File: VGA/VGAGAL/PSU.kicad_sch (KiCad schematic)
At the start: 33 parts, among them U10 74LVC10, U11 74LVC11, U12 SN74LVC86, U16 74VLC1008, U17 74LVC139, U18 74LVC11, U19 74LVC00, U2 74ALVC04, U25 74LVC21, U3 74LVC1G332, U34 74LVC1G32, U4 74VLC1032, U5 L78L33_TO92, U6 74LVC21, U7 74VLC04

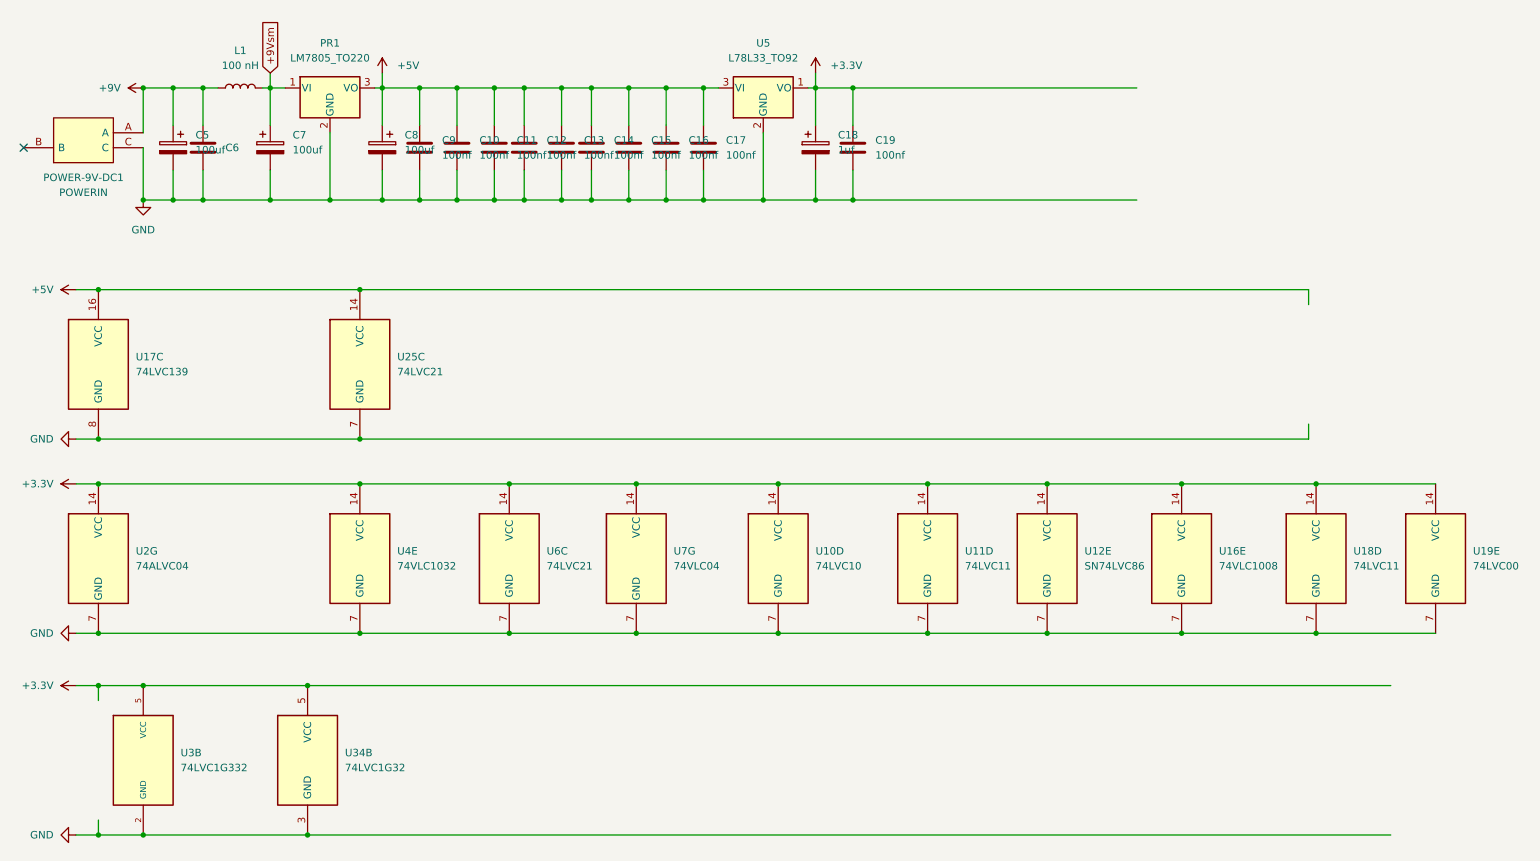
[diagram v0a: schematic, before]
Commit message: Some ideas on VGA.
Signed-off-by: John Bradley <flypie@rocketmail.com>
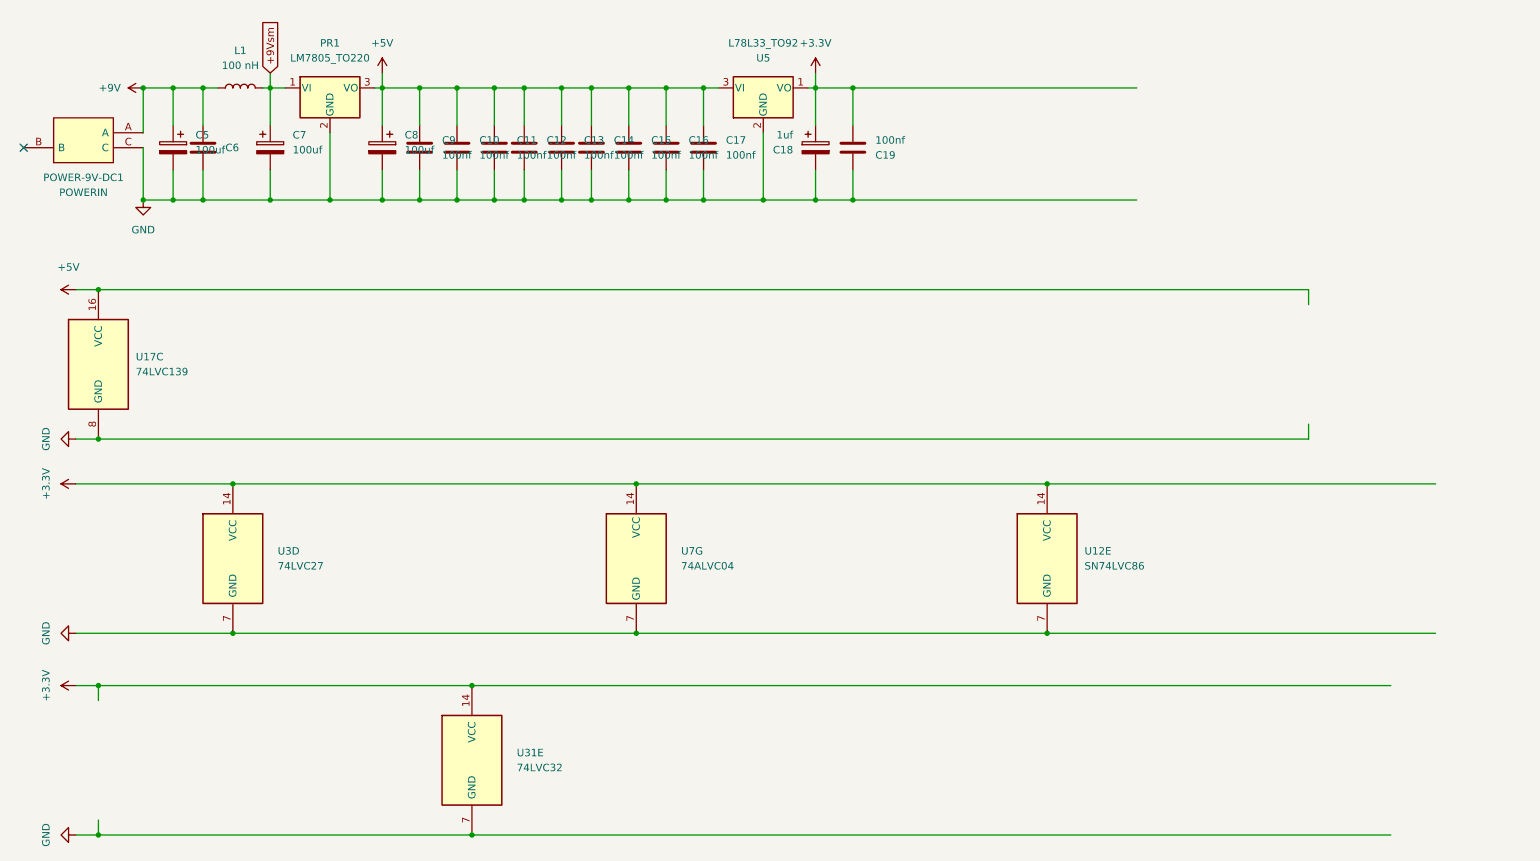
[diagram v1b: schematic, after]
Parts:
- removed U10: 74LVC10, Package_SO:SOIC-14_3.9x8.7mm_P1.27mm, symbol 74xx-FIX:74LS10
- removed U11, U18: 74LVC11, Package_SO:SOIC-14_3.9x8.7mm_P1.27mm, symbol 74xx:74LS11
- removed U16: 74VLC1008, Package_SO:SOIC-14_3.9x8.7mm_P1.27mm, symbol 74xx:74LS08
- removed U19: 74LVC00, Package_SO:SOIC-14_3.9x8.7mm_P1.27mm, symbol 74xx:74LS00
- removed U2: 74ALVC04, Package_SO:SOIC-14_3.9x8.7mm_P1.27mm, symbol 74xx:74LS04
- removed U25, U6: 74LVC21, Package_SO:SOIC-14_3.9x8.7mm_P1.27mm, symbol 74xx-FIX:74LS21
- removed U34: 74LVC1G32, Package_SO:TSOP-5_1.65x3.05mm_P0.95mm, symbol ExtraSymbols:74LVC1G32
- removed U4: 74VLC1032, Package_SO:SOIC-14_3.9x8.7mm_P1.27mm, symbol 74xx-FIX:74LS32
- added U31: 74LVC32, Package_SO:SOIC-14_3.9x8.7mm_P1.27mm, symbol 74xx-FIX:74LS32
- U3: value 74LVC1G332 -> 74LVC27; footprint Package_SO:TSOP-6_1.65x3.05mm_P0.95mm -> Package_SO:SOIC-14_3.9x8.7mm_P1.27mm; symbol 74xx-FIX:74LVC1G332 -> 74xx-FIX:74LS27
- U7: value 74VLC04 -> 74ALVC04
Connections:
- net +3.3V: now also U3.14 (VCC), U31.14 (VCC); no longer U3.5 (VCC)
- net GND: now also U3.7 (GND), U31.7 (GND); no longer U3.2 (GND)
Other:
- moved on the sheet: U3D

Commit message: Complete Move to KiCAD V6.
Plus various bits of ROM Dev and backups.

Signed-off-by: John Bradley <flypie@rocketmail.com>
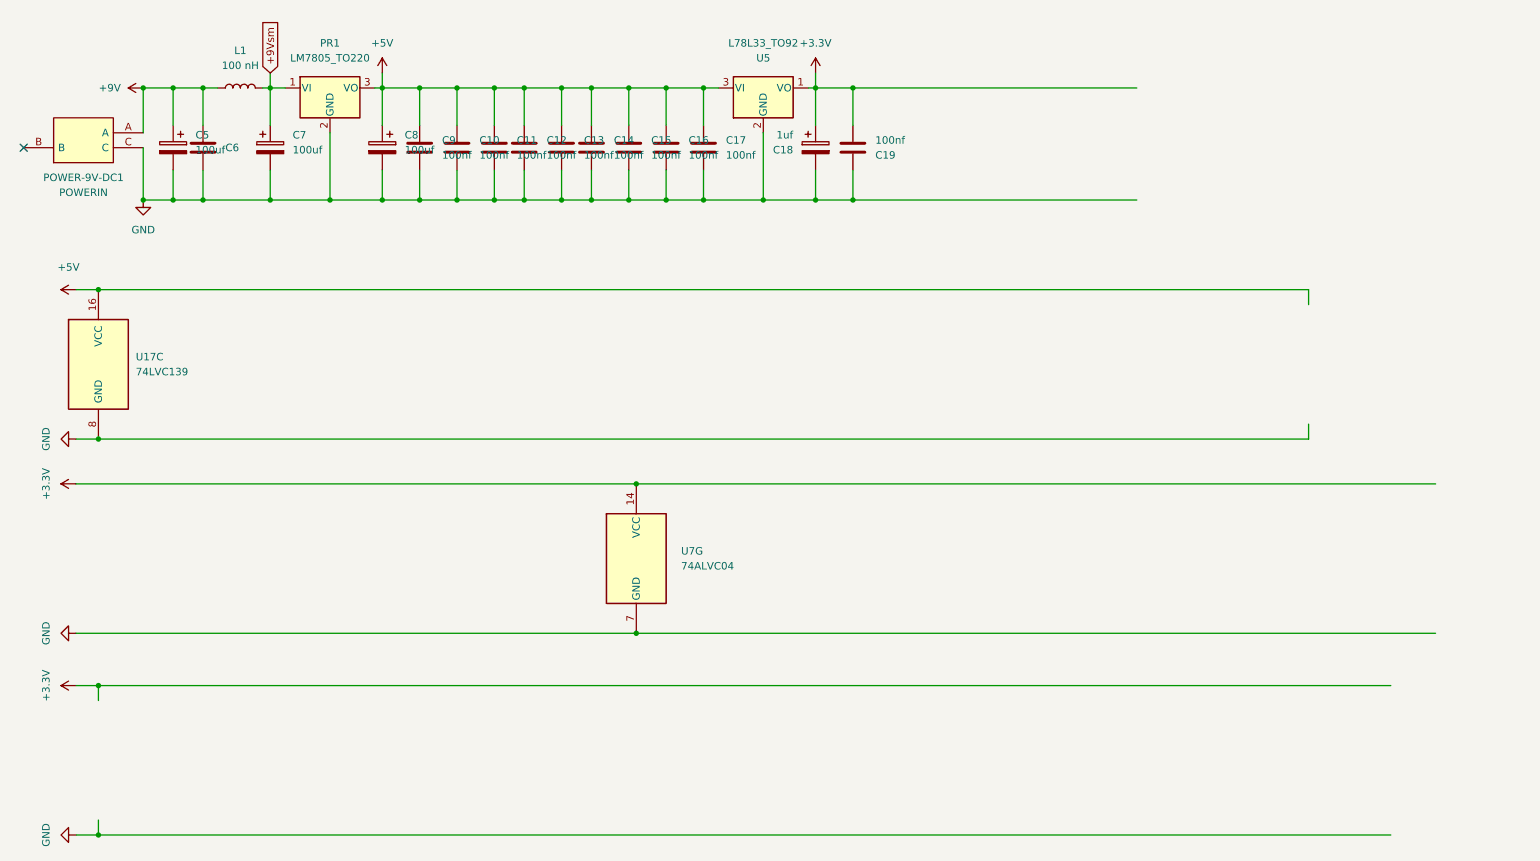
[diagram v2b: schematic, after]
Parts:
- removed U12: SN74LVC86, Package_SO:SOIC-14_3.9x8.7mm_P1.27mm, symbol 74xx:74LS86
- removed U3: 74LVC27, Package_SO:SOIC-14_3.9x8.7mm_P1.27mm, symbol 74xx-FIX:74LS27
- removed U31: 74LVC32, Package_SO:SOIC-14_3.9x8.7mm_P1.27mm, symbol 74xx-FIX:74LS32
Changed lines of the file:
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@@
   (junction (at 48.26 25.4) (diameter 0) (color 0 0 0 0)
   )
-  (junction (at 93.98 127) (diameter 0) (color 0 0 0 0)
-  )
   (junction (at 97.79 44.45) (diameter 0) (color 0 0 0 0)
   )
@@
   (junction (at 133.35 25.4) (diameter 0) (color 0 0 0 0)
   )
-  (junction (at 191.77 92.71) (diameter 0) (color 0 0 0 0)
-  )
-  (junction (at 93.98 152.4) (diameter 0) (color 0 0 0 0)
-  )
   (junction (at 158.75 44.45) (diameter 0) (color 0 0 0 0)
   )
@@
   (junction (at 91.44 25.4) (diameter 0) (color 0 0 0 0)
   )
-  (junction (at 191.77 118.11) (diameter 0) (color 0 0 0 0)
-  )
   (junction (at 102.87 25.4) (diameter 0) (color 0 0 0 0)
   )
@@
   (junction (at 48.26 44.45) (diameter 0) (color 0 0 0 0)
   )
-  (junction (at 53.34 118.11) (diameter 0) (color 0 0 0 0)
-  )
   (junction (at 69.85 44.45) (diameter 0) (color 0 0 0 0)
   )
@@
   )
   (junction (at 152.4 25.4) (diameter 0) (color 0 0 0 0)
-  )
-  (junction (at 53.34 92.71) (diameter 0) (color 0 0 0 0)
   )
   (junction (at 38.1 44.45) (diameter 0) (color 0 0 0 0)
@@
     (stroke (width 0) (type default) (color 0 0 0 0))
   )
-  (wire (pts (xy 26.67 118.11) (xy 53.34 118.11))
-    (stroke (width 0) (type default) (color 0 0 0 0))
-  )
   (wire (pts (xy 97.79 25.4) (xy 97.79 31.75))
     (stroke (width 0) (type default) (color 0 0 0 0))
@@
     (stroke (width 0) (type default) (color 0 0 0 0))
   )
-  (wire (pts (xy 121.92 92.71) (xy 191.77 92.71))
-    (stroke (width 0) (type default) (color 0 0 0 0))
-  )
   (wire (pts (xy 38.1 25.4) (xy 38.1 33.02))
     (stroke (width 0) (type default) (color 0 0 0 0))
@@
     (stroke (width 0) (type default) (color 0 0 0 0))
   )
-  (wire (pts (xy 121.92 118.11) (xy 191.77 118.11))
+  (wire (pts (xy 121.92 118.11) (xy 257.81 118.11))
     (stroke (width 0) (type default) (color 0 0 0 0))
   )
@@
     (stroke (width 0) (type default) (color 0 0 0 0))
   )
-  (wire (pts (xy 191.77 92.71) (xy 257.81 92.71))
+  (wire (pts (xy 121.92 92.71) (xy 257.81 92.71))
     (stroke (width 0) (type default) (color 0 0 0 0))
   )
@@
     (stroke (width 0) (type default) (color 0 0 0 0))
   )
-  (wire (pts (xy 30.48 127) (xy 93.98 127))
+  (wire (pts (xy 30.48 127) (xy 250.19 127))
     (stroke (width 0) (type default) (color 0 0 0 0))
   )
@@
     (stroke (width 0) (type default) (color 0 0 0 0))
   )
-  (wire (pts (xy 53.34 92.71) (xy 121.92 92.71))
+  (wire (pts (xy 26.67 92.71) (xy 121.92 92.71))
     (stroke (width 0) (type default) (color 0 0 0 0))
   )
@@
     (stroke (width 0) (type default) (color 0 0 0 0))
   )
-  (wire (pts (xy 93.98 127) (xy 250.19 127))
-    (stroke (width 0) (type default) (color 0 0 0 0))
-  )
-  (wire (pts (xy 26.67 92.71) (xy 53.34 92.71))
-    (stroke (width 0) (type default) (color 0 0 0 0))
-  )
   (wire (pts (xy 127 44.45) (xy 133.35 44.45))
     (stroke (width 0) (type default) (color 0 0 0 0))
@@
     (stroke (width 0) (type default) (color 0 0 0 0))
   )
-  (wire (pts (xy 93.98 152.4) (xy 250.19 152.4))
-    (stroke (width 0) (type default) (color 0 0 0 0))
-  )
   (wire (pts (xy 38.1 25.4) (xy 43.18 25.4))
     (stroke (width 0) (type default) (color 0 0 0 0))
@@
     (stroke (width 0) (type default) (color 0 0 0 0))
   )
-  (wire (pts (xy 30.48 152.4) (xy 93.98 152.4))
+  (wire (pts (xy 30.48 152.4) (xy 250.19 152.4))
     (stroke (width 0) (type default) (color 0 0 0 0))
   )
@@
     (stroke (width 0) (type default) (color 0 0 0 0))
   )
-  (wire (pts (xy 53.34 118.11) (xy 121.92 118.11))
-    (stroke (width 0) (type default) (color 0 0 0 0))
-  )
-  (wire (pts (xy 191.77 118.11) (xy 257.81 118.11))
+  (wire (pts (xy 26.67 118.11) (xy 121.92 118.11))
     (stroke (width 0) (type default) (color 0 0 0 0))
   )
@@
     (pin "1")
     (pin "2")
-  )
-  (symbol (lib_id "74xx-FIX:74LS32") (at 93.98 139.7 0) (unit 5)
-    (in_bom yes) (on_board yes) (fields_autoplaced)
-    (property "Reference" "U31" (id 0) (at 101.6 138.4299 0)
-      (effects (font (size 1.27 1.27)) (justify left))
-    )
-    (property "Value" "74LVC32" (id 1) (at 101.6 140.9699 0)
-      (effects (font (size 1.27 1.27)) (justify left))
-    )
-    (property "Footprint" "Package_SO:SOIC-14_3.9x8.7mm_P1.27mm" (id 2) (at 93.98 139.7 0)
-      (effects (font (size 1.27 1.27)) hide)
-    )
-    (property "Datasheet" "http://www.ti.com/lit/gpn/sn74LS32" (id 3) (at 93.98 139.7 0)
-      (effects (font (size 1.27 1.27)) hide)
-    )
-    (pin "1")
-    (pin "2")
-    (pin "3")
-    (pin "4")
-    (pin "5")
-    (pin "6")
-    (pin "10")
-    (pin "8")
-    (pin "9")
-    (pin "11")
-    (pin "12")
-    (pin "13")
-    (pin "14")
-    (pin "7")
   )
   (symbol (lib_id "Device:C") (at 158.75 35.56 0) (mirror y) (unit 1)
@@
     (pin "1")
   )
-  (symbol (lib_id "74xx:74LS86") (at 191.77 105.41 0) (unit 5)
-    (in_bom yes) (on_board yes) (fields_autoplaced)
-    (property "Reference" "U12" (id 0) (at 198.12 104.1399 0)
-      (effects (font (size 1.27 1.27)) (justify left))
-    )
-    (property "Value" "SN74LVC86" (id 1) (at 198.12 106.6799 0)
-      (effects (font (size 1.27 1.27)) (justify left))
-    )
-    (property "Footprint" "Package_SO:SOIC-14_3.9x8.7mm_P1.27mm" (id 2) (at 191.77 105.41 0)
-      (effects (font (size 1.27 1.27)) hide)
-    )
-    (property "Datasheet" "74xx/74ls86.pdf" (id 3) (at 191.77 105.41 0)
-      (effects (font (size 1.27 1.27)) hide)
-    )
-    (property "Manufacturer_Part_Number" "SN74AHCT86N" (id 4) (at 191.77 105.41 0)
-      (effects (font (size 1.27 1.27)) hide)
-    )
-    (property "Manufacturer_Name" "Texas Instruments" (id 5) (at 191.77 105.41 0)
-      (effects (font (size 1.27 1.27)) hide)
-    )
-    (pin "1")
-    (pin "2")
-    (pin "3")
-    (pin "4")
-    (pin "5")
-    (pin "6")
-    (pin "10")
-    (pin "8")
-    (pin "9")
-    (pin "11")
-    (pin "12")
-    (pin "13")
-    (pin "14")
-    (pin "7")
-  )
   (symbol (lib_id "power:+9V") (at 38.1 25.4 90) (unit 1)
     (in_bom yes) (on_board yes) (fields_autoplaced)
@@
     (pin "3")
   )
-  (symbol (lib_id "74xx-FIX:74LS27") (at 53.34 105.41 0) (unit 4)
-    (in_bom yes) (on_board yes) (fields_autoplaced)
-    (property "Reference" "U3" (id 0) (at 60.96 104.1399 0)
-      (effects (font (size 1.27 1.27)) (justify left))
-    )
-    (property "Value" "74LVC27" (id 1) (at 60.96 106.6799 0)
-      (effects (font (size 1.27 1.27)) (justify left))
-    )
-    (property "Footprint" "Package_SO:SOIC-14_3.9x8.7mm_P1.27mm" (id 2) (at 53.34 105.41 0)
-      (effects (font (size 1.27 1.27)) hide)
-    )
-    (property "Datasheet" "https://www.ti.com/product/CD74HCT27" (id 3) (at 53.34 105.41 0)
-      (effects (font (size 1.27 1.27)) hide)
-    )
-    (pin "1")
-    (pin "12")
-    (pin "13")
-    (pin "2")
-    (pin "3")
-    (pin "4")
-    (pin "5")
-    (pin "6")
-    (pin "10")
-    (pin "11")
-    (pin "8")
-    (pin "9")
-    (pin "14")
-    (pin "7")
-  )
   (symbol (lib_id "Device:C") (at 120.65 35.56 0) (unit 1)
